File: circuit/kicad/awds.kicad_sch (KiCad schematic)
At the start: 4 parts, among them U1 ESP32-DevKitC

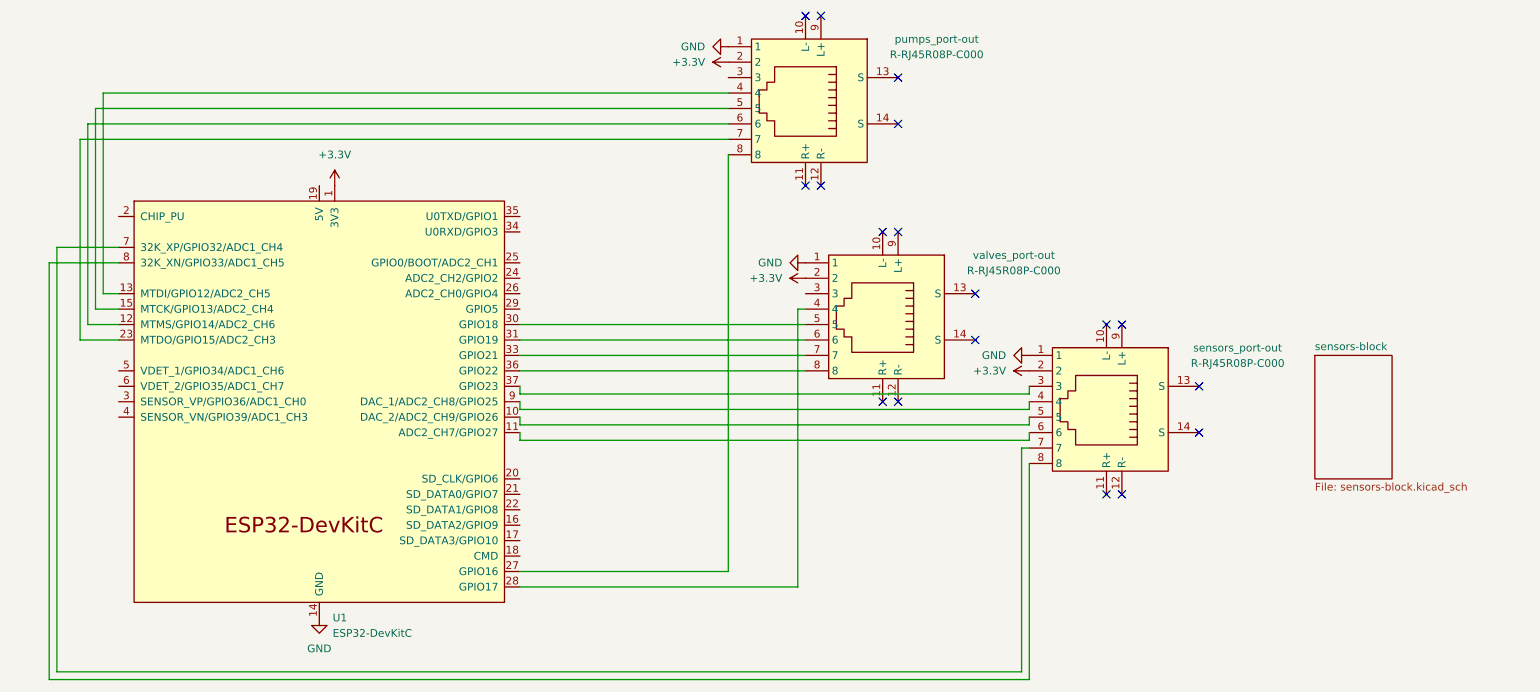
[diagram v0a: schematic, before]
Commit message: Added Command Module Circuit
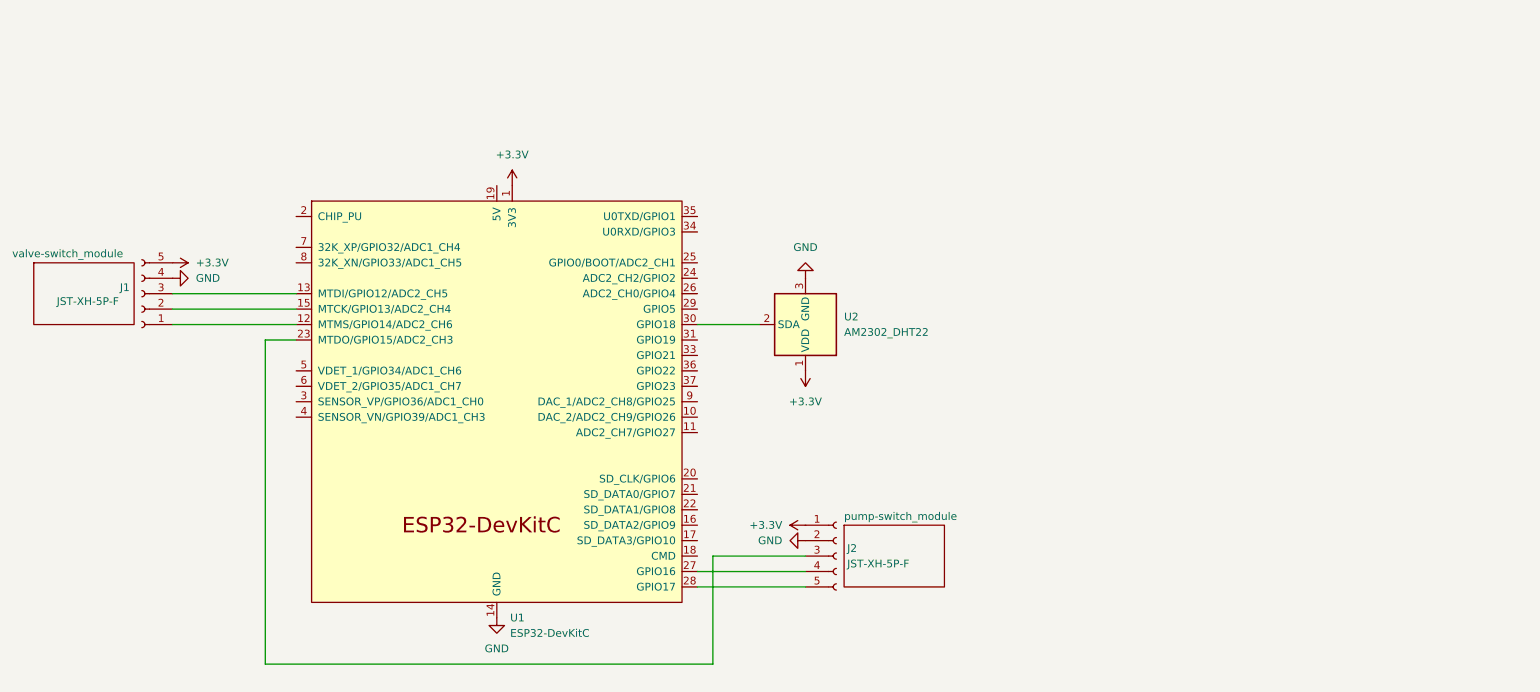
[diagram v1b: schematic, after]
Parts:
- removed pumps_port-out, sensors_port-out, valves_port-out: R-RJ45R08P-C000, easyeda2kicad:RJ45-TH_R-RJ45R08P-C000, symbol easyeda2kicad:R-RJ45R08P-C000
- added J1, J2: JST-XH-5P-F, symbol Connector:Conn_01x05_Socket
- added U2: AM2302_DHT22, Sensor:ASAIR_AM2302_P2.54mm_Vertical, symbol Sensor:AM2302
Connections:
- net +3.3V: now also J1.5 (Pin_5), J2.1 (Pin_1), U2.1 (VDD)
- net GND: now also J1.4 (Pin_4), J2.2 (Pin_2), U2.3 (GND), U2.4 (GND)
- net at U1.28 (GPIO17): now also J2.5 (Pin_5)
- net at U1.30 (GPIO18): now also U2.2 (SDA)
- net at U1.12 (MTMS/GPIO14/ADC2_CH6): now also J1.1 (Pin_1)
- net at U1.13 (MTDI/GPIO12/ADC2_CH5): now also J1.3 (Pin_3)
- net at U1.15 (MTCK/GPIO13/ADC2_CH4): now also J1.2 (Pin_2)
- net at U1.23 (MTDO/GPIO15/ADC2_CH3): now also J2.3 (Pin_3)
- net at U1.27 (GPIO16): now also J2.4 (Pin_4)
- no-connect marks 18 -> 0
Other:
- removed sheet sensors-block
- added sheet pump-switch_module (pump-switch_module.kicad_sch)
- added sheet valve-switch_module (valve-switch_module.kicad_sch)
- company: (none) -> SAM DIXON
- title: CIRCUIT - AWDS -> COMMAND MODULE - AWDS CIRCUIT
- moved on the sheet: U1

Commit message: Updated Circuit
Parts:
- added BT1: battery-12v, symbol Device:Battery
- added J10, J14, J3, J4, J5, J6: JST-PH-2P-F, symbol Connector:Conn_01x02_Socket
- added J11, J15: JST-PH-2P-M, symbol Connector:Conn_01x02_Pin
- added J12, J7: JST-PH-5P-F, symbol Connector:Conn_01x05_Socket
- added J13, J8: JST-PH-5P-M, symbol Connector:Conn_01x05_Pin
- added K1, K2, K3, K4: SANYOU_SRD_Form_C, Relay_THT:Relay_SPDT_SANYOU_SRD_Series_Form_C, symbol Relay:SANYOU_SRD_Form_C
- added U3: 74HC595, symbol 74xx:74HC595
- added U4: buck-cnv-board_12v-3.3v, symbol Regulator_Switching:XL1509-3.3
- J1, J2: value JST-XH-5P-F -> JST-PH-5P-F
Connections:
- net +3.3V: now also J1.1 (Pin_1), U4.3 (VOUT); no longer J1.5 (Pin_5)
- net GND: now also J1.2 (Pin_2), U4.4 (GND); no longer J1.4 (Pin_4)
- net at U1.12 (MTMS/GPIO14/ADC2_CH6): now also J1.5 (Pin_5); no longer J1.1 (Pin_1)
- net at U1.15 (MTCK/GPIO13/ADC2_CH4): now also J1.4 (Pin_4); no longer J1.2 (Pin_2)
- new net: BT1.1 (+), J10.1 (Pin_1), U4.1 (VIN)
- new net: BT1.2 (-), J10.2 (Pin_2), U4.2 (GND)
- new net: J7.1 (Pin_1), J7.2 (Pin_2), J7.3 (Pin_3), J7.4 (Pin_4), J8.1 (Pin_1), J8.2 (Pin_2), J8.3 (Pin_3), J8.4 (Pin_4), U3.11 (SRCLK), U3.14 (SER), U3.16 (VCC), U3.8 (GND)
- new net: J7.5 (Pin_5), J8.5 (Pin_5), U3.12 (RCLK)
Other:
- removed sheet pump-switch_module
- removed sheet valve-switch_module
- note added: "+12V"
- note added: "+3.3V"
- note added: "AWDS CIRCUIT"
- note added: "COMMAND MODULE"
- note added: "DATA"
- note added: "GND"
- note added: "HEADERS"
- note added: "IN"
- note added: "OUT"
- note added: "POWER"
- note added: "RCLK"
- note added: "SRCLK"
- note added: "SWITCH MODULE"
- title: COMMAND MODULE - AWDS CIRCUIT -> AWDS CIRCUIT
- moved on the sheet: J2, U1, U2

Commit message: Added Switches and LED to Circuit
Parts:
- added D1: LED, symbol Device:LED
- added SW2, SW3: SW_DIP_x01, symbol Switch:SW_DIP_x01
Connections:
- net +3.3V: now also SW3.2
- net GND: now also D1.1 (K)
- net at J10.1 (Pin_1), U4.1 (VIN): now also SW2.2; no longer BT1.1 (+)
- net at U1.31 (GPIO19): now also SW3.1
- net at U1.33 (GPIO21): now also D1.2 (A)
- new net: BT1.1 (+), SW2.1
- new net: J7.1 (Pin_1), J8.1 (Pin_1), U3.16 (VCC)
- new net: J7.2 (Pin_2), J8.2 (Pin_2), U3.8 (GND)
- new net: J7.3 (Pin_3), J8.3 (Pin_3), U3.14 (SER)
- new net: J7.4 (Pin_4), J8.4 (Pin_4), U3.11 (SRCLK)
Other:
- moved on the sheet: U2

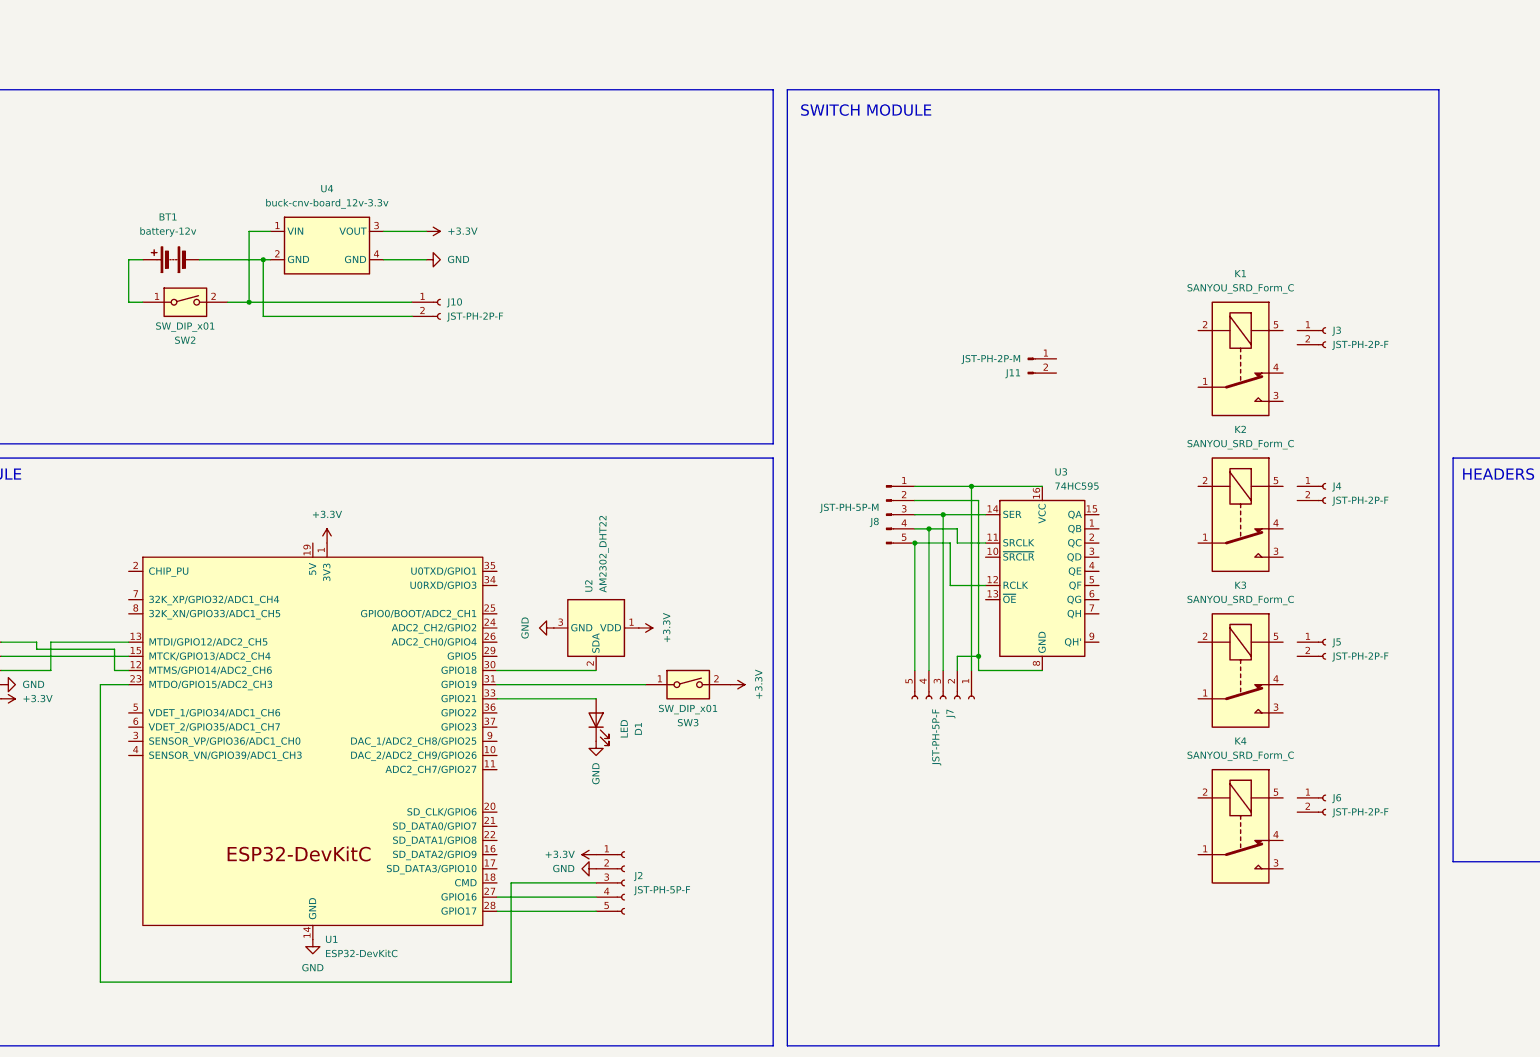
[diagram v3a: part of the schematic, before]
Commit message: Updated Component Orders with Exact Electronic Components
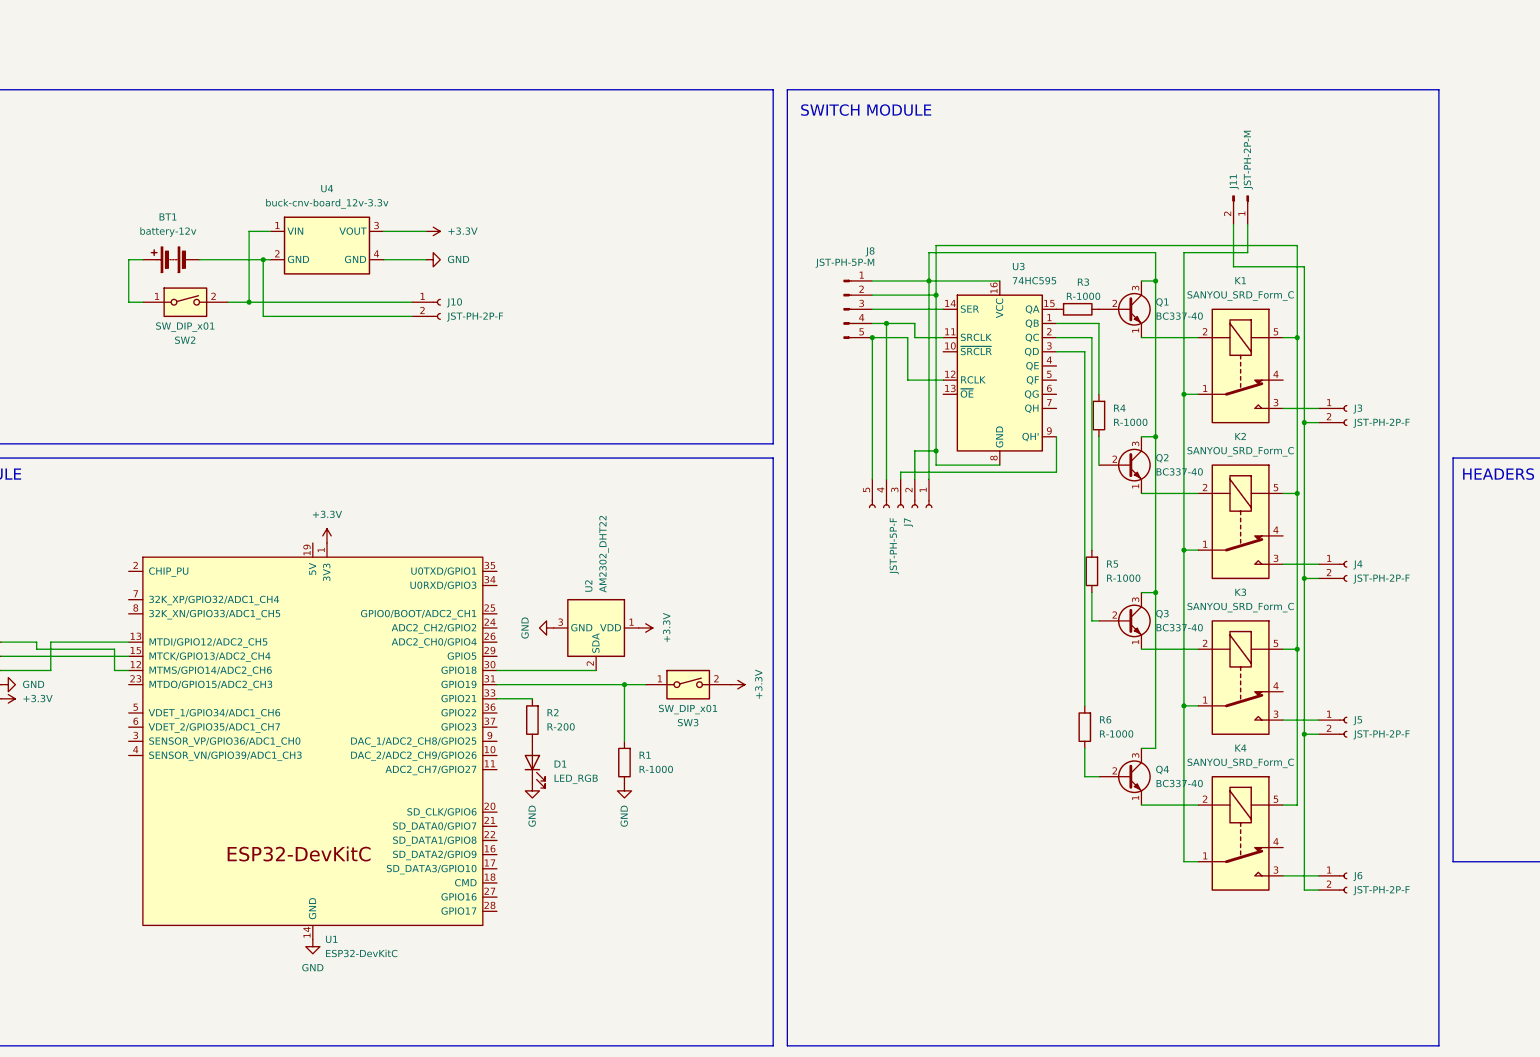
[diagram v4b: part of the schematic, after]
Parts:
- removed J2: JST-PH-5P-F, symbol Connector:Conn_01x05_Socket
- added Q1, Q2, Q3, Q4: BC337-40, symbol Transistor_BJT:BC107
- added R1, R3, R4, R5, R6: R-1000, symbol Device:R
- added R2: R-200, symbol Device:R
- D1: value LED -> LED_RGB
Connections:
- net GND: now also R1.1
- net at J3.1 (Pin_1): now also K1.3
- net at J3.2 (Pin_2): now also J11.2 (Pin_2), J4.2 (Pin_2), J5.2 (Pin_2), J6.2 (Pin_2)
- net at D1.2 (A): now also R2.1; no longer U1.33 (GPIO21)
- net at J7.1 (Pin_1), J8.1 (Pin_1), U3.16 (VCC): now also Q1.3 (C), Q2.3 (C), Q3.3 (C), Q4.3 (C)
- net at J7.2 (Pin_2), J8.2 (Pin_2), U3.8 (GND): now also K1.5, K2.5, K3.5, K4.5
- net at J8.3 (Pin_3), U3.14 (SER): no longer J7.3 (Pin_3)
- net at K1.1: now also J11.1 (Pin_1), K2.1, K3.1, K4.1
- net at K1.2: now also Q1.1 (E)
- net at K3.2: now also Q3.1 (E)
- net at K3.3: now also J5.1 (Pin_1)
- net at K2.2: now also Q2.1 (E)
- net at K2.3: now also J4.1 (Pin_1)
- net at SW3.1, U1.31 (GPIO19): now also R1.2
- net at K4.2: now also Q4.1 (E)
- net at K4.3: now also J6.1 (Pin_1)
- net at U3.1 (QB): now also R4.2
- net at U3.15 (QA): now also R3.2
- net at U3.2 (QC): now also R5.2
- net at U3.3 (QD): now also R6.2
- net at U3.9 (QH'): now also J7.3 (Pin_3)
- new net: Q3.2 (B), R5.1
- new net: Q4.2 (B), R6.1
- new net: R2.2, U1.33 (GPIO21)
- new net: Q1.2 (B), R3.1
- new net: Q2.2 (B), R4.1
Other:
- moved on the sheet: J11, J3, J4, J5, J6, J7, J8, K1, K2, K3, K4, U3
